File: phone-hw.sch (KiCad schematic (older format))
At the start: 42 parts

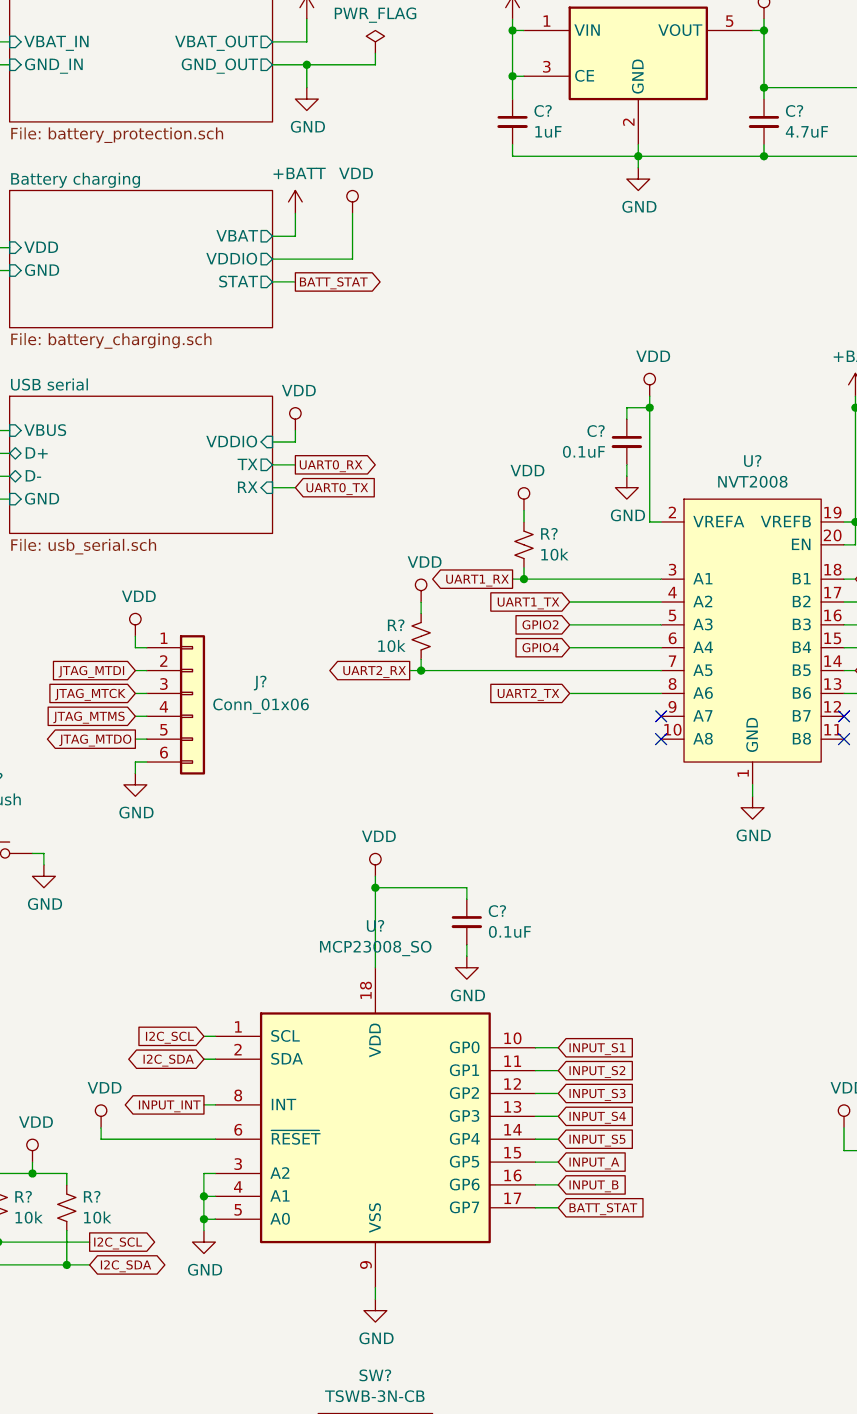
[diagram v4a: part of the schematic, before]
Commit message: upgrade charge circuit to use tp4056, allowing the battery to charge faster without the charger throttling itself
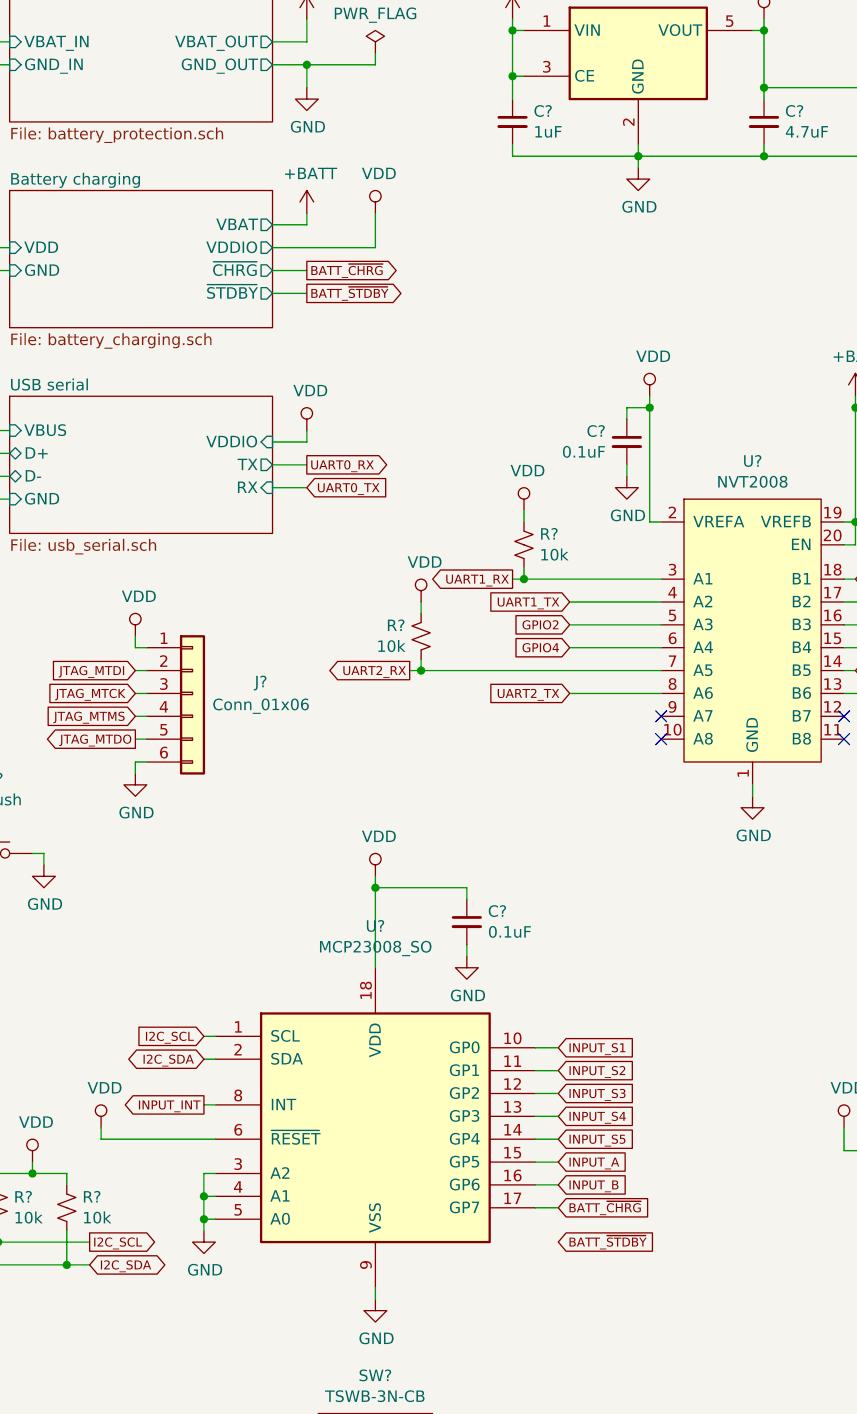
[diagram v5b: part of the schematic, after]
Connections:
- net BATT_STAT renamed BATT_~CHRG
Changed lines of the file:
@@
 F0 "Battery charging" 50
 F1 "battery_charging.sch" 50
-F2 "STAT" O R 4150 2100 50
 F3 "VDD" I L 3000 1950 50
-F4 "VBAT" O R 4150 1900 50
+F4 "VBAT" O R 4150 1850 50
 F5 "GND" I L 3000 2050 50
-F6 "VDDIO" O R 4150 2000 50
+F6 "VDDIO" O R 4150 1950 50
+F7 "~STDBY" O R 4150 2150 50
+F8 "~CHRG" O R 4150 2050 50
 $EndSheet
 $Comp
@@
 L power:+BATT #PWR?
 U 1 1 5C93D731
-P 4250 1800
-F 0 "#PWR?" H 4250 1650 50  0001 C CNN
-F 1 "+BATT" H 4265 1973 50  0000 C CNN
-F 2 "" H 4250 1800 50  0001 C CNN
-F 3 "" H 4250 1800 50  0001 C CNN
-	1    4250 1800
-	1    0    0    -1
-$EndComp
-Wire Wire Line
-	4150 1900 4250 1900
-Wire Wire Line
-	4250 1900 4250 1800
-Text GLabel 4250 2100 2    39   Output ~ 0
-BATT_STAT
-Wire Wire Line
-	4150 2100 4250 2100
+P 4300 1800
+F 0 "#PWR?" H 4300 1650 50  0001 C CNN
+F 1 "+BATT" H 4315 1973 50  0000 C CNN
+F 2 "" H 4300 1800 50  0001 C CNN
+F 3 "" H 4300 1800 50  0001 C CNN
+	1    4300 1800
+	1    0    0    -1
+$EndComp
+Wire Wire Line
+	4150 1850 4300 1850
+Wire Wire Line
+	4300 1850 4300 1800
+Text GLabel 4300 2050 2    39   Output ~ 0
+BATT_~CHRG
+Wire Wire Line
+	4150 2050 4300 2050
 $Comp
 L power:GND #PWR?
@@
 L power:VDD #PWR?
 U 1 1 5C94ACAC
-P 4250 2750
-F 0 "#PWR?" H 4250 2600 50  0001 C CNN
-F 1 "VDD" H 4267 2923 50  0000 C CNN
-F 2 "" H 4250 2750 50  0001 C CNN
-F 3 "" H 4250 2750 50  0001 C CNN
-	1    4250 2750
-	1    0    0    -1
-$EndComp
-Wire Wire Line
-	4250 2750 4250 2800
-Wire Wire Line
-	4250 2800 4150 2800
-Text GLabel 4250 2900 2    39   Output ~ 0
+P 4300 2750
+F 0 "#PWR?" H 4300 2600 50  0001 C CNN
+F 1 "VDD" H 4317 2923 50  0000 C CNN
+F 2 "" H 4300 2750 50  0001 C CNN
+F 3 "" H 4300 2750 50  0001 C CNN
+	1    4300 2750
+	1    0    0    -1
+$EndComp
+Wire Wire Line
+	4300 2750 4300 2800
+Wire Wire Line
+	4300 2800 4150 2800
+Text GLabel 4300 2900 2    39   Output ~ 0
 UART0_RX
-Text GLabel 4250 3000 2    39   Input ~ 0
+Text GLabel 4300 3000 2    39   Input ~ 0
 UART0_TX
 Wire Wire Line
-	4150 3000 4250 3000
-Wire Wire Line
-	4250 2900 4150 2900
+	4150 3000 4300 3000
+Wire Wire Line
+	4300 2900 4150 2900
 $Comp
 L phone:XC6222B281MR-G U?
@@
 	2000 1800 2000 1700
 Connection ~ 1650 1800
-Text GLabel 5400 6150 2    39   Input ~ 0
-BATT_STAT
 Wire Wire Line
 	3150 4600 3150 4650
@@
 L power:VDD #PWR?
 U 1 1 5CE29625
-P 4500 1800
-F 0 "#PWR?" H 4500 1650 50  0001 C CNN
-F 1 "VDD" H 4517 1973 50  0000 C CNN
-F 2 "" H 4500 1800 50  0001 C CNN
-F 3 "" H 4500 1800 50  0001 C CNN
-	1    4500 1800
-	1    0    0    -1
-$EndComp
-Wire Wire Line
-	4150 2000 4500 2000
-Wire Wire Line
-	4500 2000 4500 1800
+P 4600 1800
+F 0 "#PWR?" H 4600 1650 50  0001 C CNN
+F 1 "VDD" H 4617 1973 50  0000 C CNN
+F 2 "" H 4600 1800 50  0001 C CNN
+F 3 "" H 4600 1800 50  0001 C CNN
+	1    4600 1800
+	1    0    0    -1
+$EndComp
+Wire Wire Line
+	4150 1950 4600 1950
+Wire Wire Line
+	4600 1950 4600 1800
 $Comp
 L Device:Q_NPN_BEC Q?
@@
 	1    0    0    -1
 $EndComp
+Text GLabel 4300 2150 2    39   Output ~ 0
+BATT_~STDBY
+Wire Wire Line
+	4150 2150 4300 2150
+Text GLabel 5400 6150 2    39   Input ~ 0
+BATT_~CHRG
+Text GLabel 5400 6300 2    39   Input ~ 0
+BATT_~STDBY
 $EndSCHEMATC

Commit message: set schematic to use folded display
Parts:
- U?: footprint phone:ER-TFT1.44-1 -> phone:ER-TFT1.44-1-FOLD
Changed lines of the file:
@@
 F0 "Battery charging" 50
 F1 "battery_charging.sch" 50
-F3 "VDD" I L 3000 1950 50
-F4 "VBAT" O R 4150 1850 50
-F5 "GND" I L 3000 2050 50
-F6 "VDDIO" O R 4150 1950 50
-F7 "~STDBY" O R 4150 2150 50
-F8 "~CHRG" O R 4150 2050 50
+F2 "VDD" I L 3000 1950 50
+F3 "VBAT" O R 4150 1850 50
+F4 "GND" I L 3000 2050 50
+F5 "VDDIO" O R 4150 1950 50
+F6 "~STDBY" O R 4150 2150 50
+F7 "~CHRG" O R 4150 2050 50
 $EndSheet
 $Comp
@@
 F 0 "U?" H 8350 6578 50  0000 C CNN
 F 1 "ER-TFT1.44-1" H 8350 6487 50  0000 C CNN
-F 2 "phone:ER-TFT1.44-1" H 8350 5650 50  0001 C CNN
+F 2 "phone:ER-TFT1.44-1-FOLD" H 8350 5650 50  0001 C CNN
 F 3 "" H 8350 5650 50  0001 C CNN
 	1    8350 5650

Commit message: switch i/o expander to larger version, moving signals off esp32
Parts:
- removed U?: MCP23008_SO, Package_SO:SOIC-18W_7.5x11.6mm_P1.27mm, symbol phone:MCP23008_SO
- added U?: PCAL6416A, symbol phone:PCAL6416A
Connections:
- net BATT_~CHRG: now also U?.11 (P0_7)
- net BATT_~STDBY: now also U?.13 (P1_0)
- net GND: now also U?.12 (VSS), U?.21 (ADDR)
- net I2C_SCL: now also U?.22 (SCL)
- net I2C_SDA: now also U?.23 (SDA)
- net INPUT_A: now also U?.9 (P0_5)
- net INPUT_B: now also U?.10 (P0_6)
- net INPUT_INT: now also U?.5 (SENSOR_VN), U?.1 (~INT); no longer U?.12 (IO27)
- net INPUT_S1: now also U?.4 (P0_0)
- net INPUT_S2: now also U?.5 (P0_1)
- net INPUT_S3: now also U?.6 (P0_2)
- net INPUT_S4: now also U?.7 (P0_3)
- net INPUT_S5: now also U?.8 (P0_4)
- net LCD_BL: now also U?.18 (P1_5); no longer U?.9 (IO33)
- net LCD_RESET: now also U?.17 (P1_4); no longer U?.8 (IO32)
- net VDD: now also U?.2 (VDD_I2C), U?.24 (VDD_P), U?.3 (~RESET)
- net GPIO2: no longer names the net of U?.24 (IO2)
- net GPIO2: no longer U?.5 (A3)
- net GPIO4: no longer names the net of U?.26 (IO4)
- net GPIO4: no longer U?.6 (A4)
- net GPS_PPS: no longer names the net of U?.6 (1PPS)
- net GPS_PPS: no longer U?.5 (SENSOR_VN)
- new net GPS_RESET_2.8: U?.19 (P1_6), U?.5 (A3)
- new net GSM_PWRKEY_2.8: U?.20 (P1_7), U?.6 (A4)
- no-connect marks 12 -> 13
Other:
- moved on the sheet: C?, SW?

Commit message: add buttons and connect pcm interface of modem to esp32
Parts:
- added SW?: Lock, Button_Switch_SMD:SW_SPST_EVQPE1, symbol Switch:SW_Push
- added SW?: VolUp, Button_Switch_SMD:SW_SPST_EVQPE1, symbol Switch:SW_Push
- added SW?: VolDown, Button_Switch_SMD:SW_SPST_EVQPE1, symbol Switch:SW_Push
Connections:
- net GND: now also SW?.2, SW?.2, SW?.2
- net PCM_CLK: now reaches U?.12 (IO27)
- net PCM_SYNC: now reaches U?.26 (IO4)
- net PCM_IN: now reaches U?.8 (IO32)
- net PCM_OUT: now reaches U?.9 (IO33)
- net at U?.14 (P1_1): now also SW?.1
- net at U?.15 (P1_2): now also SW?.1
- net at U?.16 (P1_3): now also SW?.1
- no-connect marks 13 -> 14
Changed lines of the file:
@@
 Wire Wire Line
 	5450 6700 5550 6700
+Text GLabel 2550 6500 2    39   Output ~ 0
+PCM_CLK
+Text GLabel 2550 5000 2    39   Output ~ 0
+PCM_SYNC
+Text GLabel 2550 6600 2    39   Output ~ 0
+PCM_IN
+Text GLabel 2550 6700 2    39   Input ~ 0
+PCM_OUT
+Wire Wire Line
+	5450 6400 6050 6400
+$Comp
+L Switch:SW_Push SW?
+U 1 1 5D9343D0
+P 6650 6500
+F 0 "SW?" H 6650 6825 50  0000 C CNN
+F 1 "VolUp" H 6650 6734 50  0000 C CNN
+F 2 "Button_Switch_SMD:SW_SPST_EVQPE1" H 6650 6500 50  0001 C CNN
+F 3 "~" H 6650 6500 50  0001 C CNN
+	1    6650 6500
+	1    0    0    -1
+$EndComp
+$Comp
+L power:GND #PWR?
+U 1 1 5D950C6B
+P 7500 6550
+F 0 "#PWR?" H 7500 6300 50  0001 C CNN
+F 1 "GND" H 7505 6377 50  0000 C CNN
+F 2 "" H 7500 6550 50  0001 C CNN
+F 3 "" H 7500 6550 50  0001 C CNN
+	1    7500 6550
+	1    0    0    -1
+$EndComp
+Wire Wire Line
+	5450 6500 6450 6500
+$Comp
+L Switch:SW_Push SW?
+U 1 1 5D9897BE
+P 7100 6600
+F 0 "SW?" H 7100 6925 50  0000 C CNN
+F 1 "VolDown" H 7100 6834 50  0000 C CNN
+F 2 "Button_Switch_SMD:SW_SPST_EVQPE1" H 7100 6600 50  0001 C CNN
+F 3 "~" H 7100 6600 50  0001 C CNN
+	1    7100 6600
+	1    0    0    -1
+$EndComp
+Wire Wire Line
+	5450 6600 6900 6600
+Wire Wire Line
+	6450 6400 7350 6400
+Wire Wire Line
+	7350 6400 7350 6500
+Wire Wire Line
+	7350 6600 7300 6600
+Wire Wire Line
+	6850 6500 7350 6500
+Connection ~ 7350 6500
+Wire Wire Line
+	7350 6500 7350 6600
+Wire Wire Line
+	7500 6550 7500 6500
+Wire Wire Line
+	7500 6500 7350 6500
+$Comp
+L Switch:SW_Push SW?
+U 1 1 5D917463
+P 6250 6400
+F 0 "SW?" H 6250 6725 50  0000 C CNN
+F 1 "Lock" H 6250 6634 50  0000 C CNN
+F 2 "Button_Switch_SMD:SW_SPST_EVQPE1" H 6250 6400 50  0001 C CNN
+F 3 "~" H 6250 6400 50  0001 C CNN
+	1    6250 6400
+	1    0    0    -1
+$EndComp
+NoConn ~ 2550 4800
 $EndSCHEMATC
